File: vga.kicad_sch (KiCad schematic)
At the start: 25 parts, among them J24 Component A/V

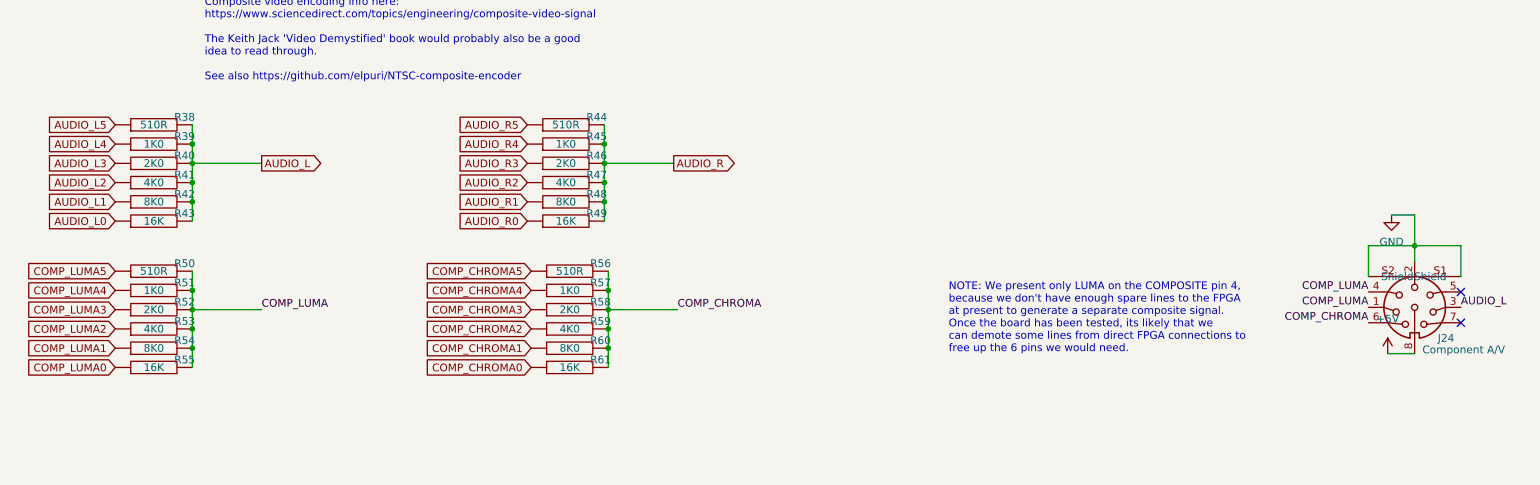
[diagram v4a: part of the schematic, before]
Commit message: reconnect everything and add PMOD and 34pin floppy connectors
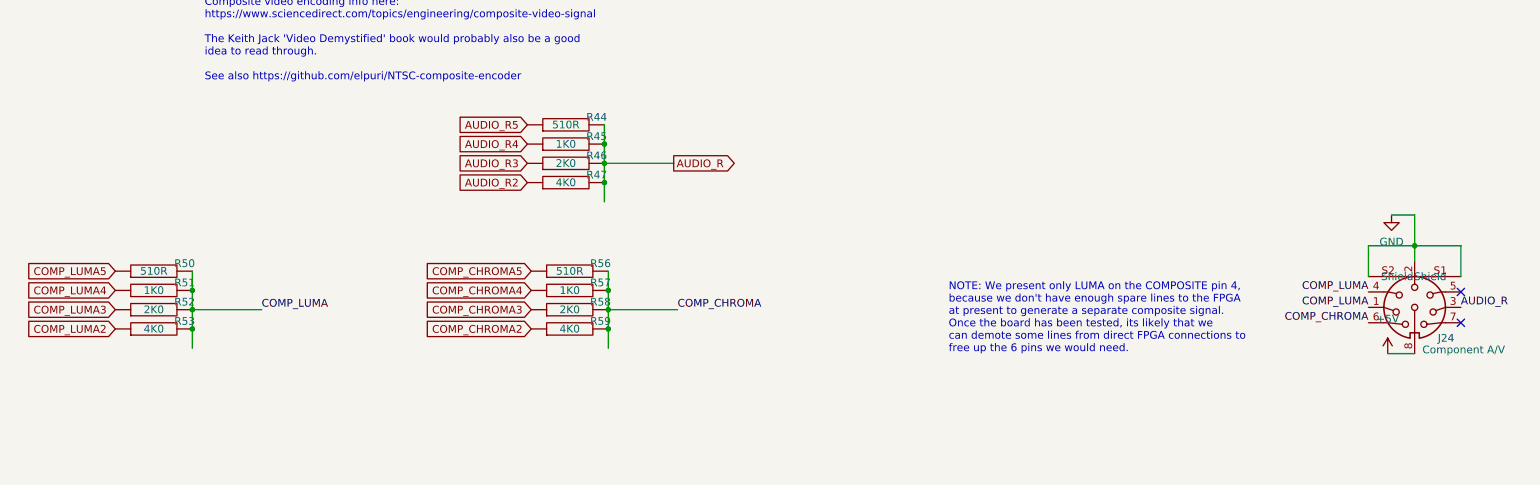
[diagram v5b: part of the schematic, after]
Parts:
- removed R38: 510R, snapeda:Labeled Resistor, symbol pspice:R
- removed R39: 1K0, snapeda:Labeled Resistor, symbol pspice:R
- removed R40: 2K0, snapeda:Labeled Resistor, symbol pspice:R
- removed R41: 4K0, snapeda:Labeled Resistor, symbol pspice:R
- removed R42, R48, R54, R60: 8K0, snapeda:Labeled Resistor, symbol pspice:R
- removed R43, R49, R55, R61: 16K, snapeda:Labeled Resistor, symbol pspice:R
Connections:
- net AUDIO_L is gone; now on net AUDIO_R: J24.3

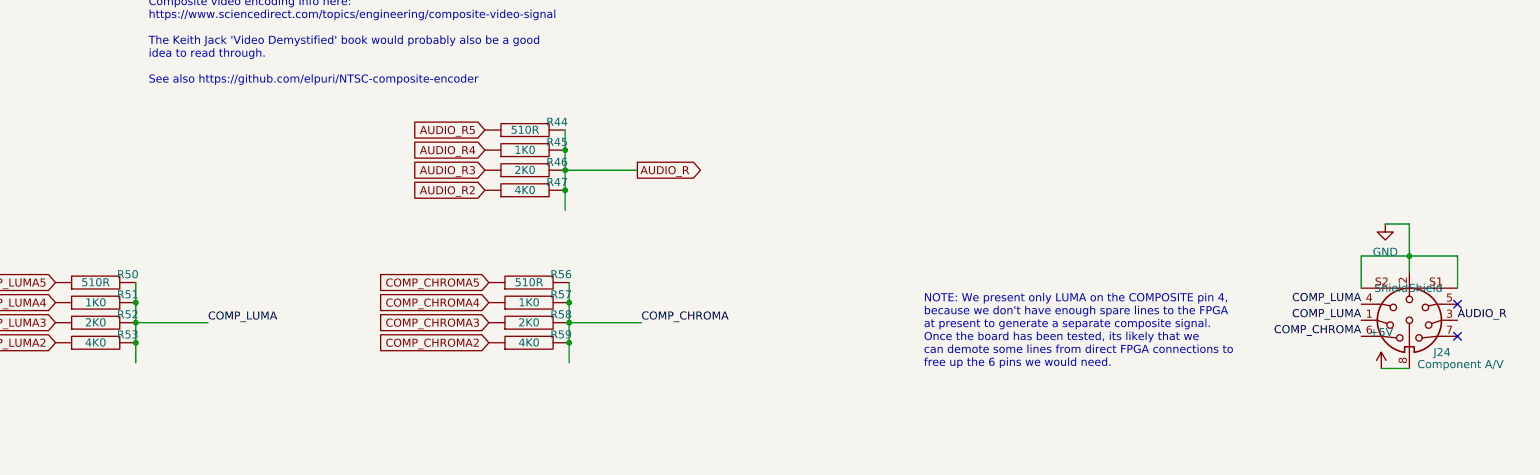
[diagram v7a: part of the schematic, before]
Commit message: work on rerouting board to fit current limiting resistors #1
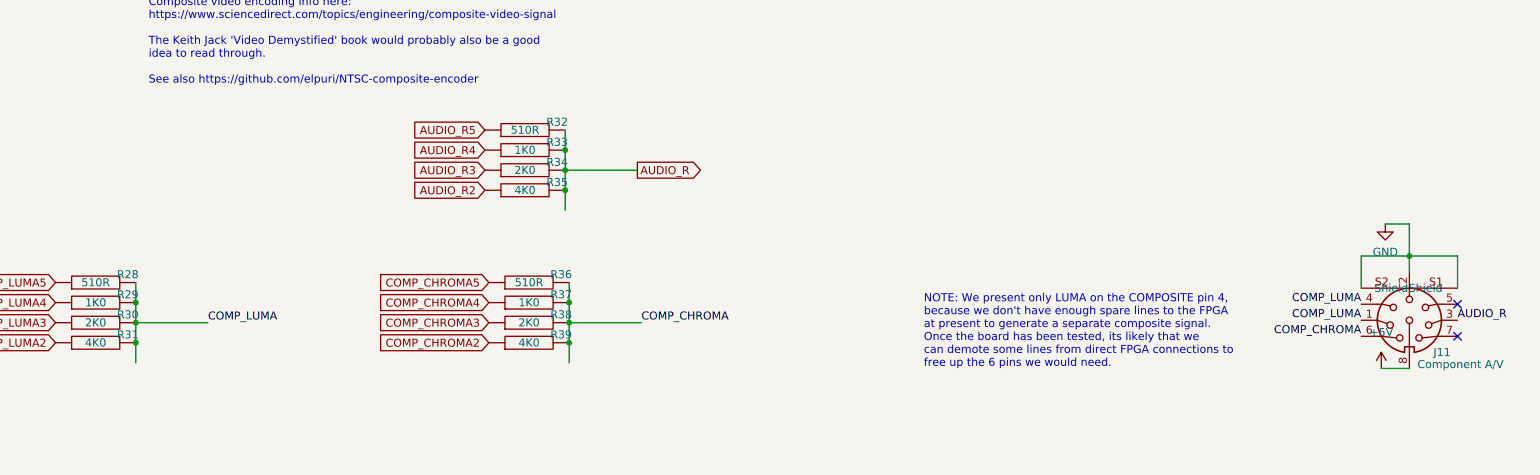
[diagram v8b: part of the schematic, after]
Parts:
- renumbered J24 to J11, R50 to R28, R51 to R29, R52 to R30, R53 to R31, R44 to R32, R45 to R33, R46 to R34, R47 to R35, R56 to R36, R57 to R37, R58 to R38, R59 to R39
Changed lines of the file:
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@@
   (symbol (lib_id "pspice:R") (at 105.41 101.6 90) (unit 1)
     (in_bom yes) (on_board yes)
-    (property "Reference" "R56" (id 0) (at 110.49 100.33 90))
+    (property "Reference" "R36" (id 0) (at 110.49 100.33 90))
     (property "Value" "510R" (id 1) (at 105.41 101.6 90))
     (property "Footprint" "snapeda:Labeled Resistor" (id 2) (at 105.41 101.6 0)
@@
   (symbol (lib_id "pspice:R") (at 36.83 107.95 90) (unit 1)
     (in_bom yes) (on_board yes)
-    (property "Reference" "R52" (id 0) (at 41.91 106.68 90))
+    (property "Reference" "R30" (id 0) (at 41.91 106.68 90))
     (property "Value" "2K0" (id 1) (at 36.83 107.95 90))
     (property "Footprint" "snapeda:Labeled Resistor" (id 2) (at 36.83 107.95 0)
@@
   (symbol (lib_id "power:+5V") (at 240.284 115.189 0) (unit 1)
     (in_bom yes) (on_board yes) (fields_autoplaced)
-    (property "Reference" "#PWR0285" (id 0) (at 240.284 118.999 0)
+    (property "Reference" "#PWR080" (id 0) (at 240.284 118.999 0)
       (effects (font (size 1.27 1.27)) hide)
     )
@@
   (symbol (lib_id "pspice:R") (at 36.83 104.775 90) (unit 1)
     (in_bom yes) (on_board yes)
-    (property "Reference" "R51" (id 0) (at 41.91 103.505 90))
+    (property "Reference" "R29" (id 0) (at 41.91 103.505 90))
     (property "Value" "1K0" (id 1) (at 36.83 104.775 90))
     (property "Footprint" "snapeda:Labeled Resistor" (id 2) (at 36.83 104.775 0)
@@
   (symbol (lib_id "pspice:R") (at 36.83 111.125 90) (unit 1)
     (in_bom yes) (on_board yes)
-    (property "Reference" "R53" (id 0) (at 41.91 109.855 90))
+    (property "Reference" "R31" (id 0) (at 41.91 109.855 90))
     (property "Value" "4K0" (id 1) (at 36.83 111.125 90))
     (property "Footprint" "snapeda:Labeled Resistor" (id 2) (at 36.83 111.125 0)
@@
   (symbol (lib_id "pspice:R") (at 104.775 77.47 90) (unit 1)
     (in_bom yes) (on_board yes)
-    (property "Reference" "R44" (id 0) (at 109.855 76.2 90))
+    (property "Reference" "R32" (id 0) (at 109.855 76.2 90))
     (property "Value" "510R" (id 1) (at 104.775 77.47 90))
     (property "Footprint" "snapeda:Labeled Resistor" (id 2) (at 104.775 77.47 0)
@@
   (symbol (lib_id "power:GND") (at 240.919 92.329 0) (unit 1)
     (in_bom yes) (on_board yes) (fields_autoplaced)
-    (property "Reference" "#PWR0283" (id 0) (at 240.919 98.679 0)
+    (property "Reference" "#PWR081" (id 0) (at 240.919 98.679 0)
       (effects (font (size 1.27 1.27)) hide)
     )
@@
   (symbol (lib_id "00Project-SDF-60J:SDF-80J") (at 244.729 107.569 0) (unit 1)
     (in_bom yes) (on_board yes)
-    (property "Reference" "J24" (id 0) (at 248.539 112.649 0)
+    (property "Reference" "J11" (id 0) (at 248.539 112.649 0)
       (effects (font (size 1.27 1.27)) (justify left))
     )
@@
   (symbol (lib_id "pspice:R") (at 104.775 83.82 90) (unit 1)
     (in_bom yes) (on_board yes)
-    (property "Reference" "R46" (id 0) (at 109.855 82.55 90))
+    (property "Reference" "R34" (id 0) (at 109.855 82.55 90))
     (property "Value" "2K0" (id 1) (at 104.775 83.82 90))
     (property "Footprint" "snapeda:Labeled Resistor" (id 2) (at 104.775 83.82 0)
@@
   (symbol (lib_id "pspice:R") (at 105.41 104.775 90) (unit 1)
     (in_bom yes) (on_board yes)
-    (property "Reference" "R57" (id 0) (at 110.49 103.505 90))
+    (property "Reference" "R37" (id 0) (at 110.49 103.505 90))
     (property "Value" "1K0" (id 1) (at 105.41 104.775 90))
     (property "Footprint" "snapeda:Labeled Resistor" (id 2) (at 105.41 104.775 0)
@@
   (symbol (lib_id "pspice:R") (at 105.41 107.95 90) (unit 1)
     (in_bom yes) (on_board yes)
-    (property "Reference" "R58" (id 0) (at 110.49 106.68 90))
+    (property "Reference" "R38" (id 0) (at 110.49 106.68 90))
     (property "Value" "2K0" (id 1) (at 105.41 107.95 90))
     (property "Footprint" "snapeda:Labeled Resistor" (id 2) (at 105.41 107.95 0)
@@
   (symbol (lib_id "pspice:R") (at 36.83 101.6 90) (unit 1)
     (in_bom yes) (on_board yes)
-    (property "Reference" "R50" (id 0) (at 41.91 100.33 90))
+    (property "Reference" "R28" (id 0) (at 41.91 100.33 90))
     (property "Value" "510R" (id 1) (at 36.83 101.6 90))
     (property "Footprint" "snapeda:Labeled Resistor" (id 2) (at 36.83 101.6 0)
@@
   (symbol (lib_id "pspice:R") (at 104.775 86.995 90) (unit 1)
     (in_bom yes) (on_board yes)
-    (property "Reference" "R47" (id 0) (at 109.855 85.725 90))
+    (property "Reference" "R35" (id 0) (at 109.855 85.725 90))
     (property "Value" "4K0" (id 1) (at 104.775 86.995 90))
     (property "Footprint" "snapeda:Labeled Resistor" (id 2) (at 104.775 86.995 0)
@@
   (symbol (lib_id "pspice:R") (at 105.41 111.125 90) (unit 1)
     (in_bom yes) (on_board yes)
-    (property "Reference" "R59" (id 0) (at 110.49 109.855 90))
+    (property "Reference" "R39" (id 0) (at 110.49 109.855 90))
     (property "Value" "4K0" (id 1) (at 105.41 111.125 90))
     (property "Footprint" "snapeda:Labeled Resistor" (id 2) (at 105.41 111.125 0)
@@
   (symbol (lib_id "pspice:R") (at 104.775 80.645 90) (unit 1)
     (in_bom yes) (on_board yes)
-    (property "Reference" "R45" (id 0) (at 109.855 79.375 90))
+    (property "Reference" "R33" (id 0) (at 109.855 79.375 90))
     (property "Value" "1K0" (id 1) (at 104.775 80.645 90))
     (property "Footprint" "snapeda:Labeled Resistor" (id 2) (at 104.775 80.645 0)
